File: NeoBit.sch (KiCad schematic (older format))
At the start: 17 parts, among them J2 Barrel_Jack_MountingPin, J5 microbit_edge_connector, U1 74AHCT125, U2 MCP1702-3302E_TO92

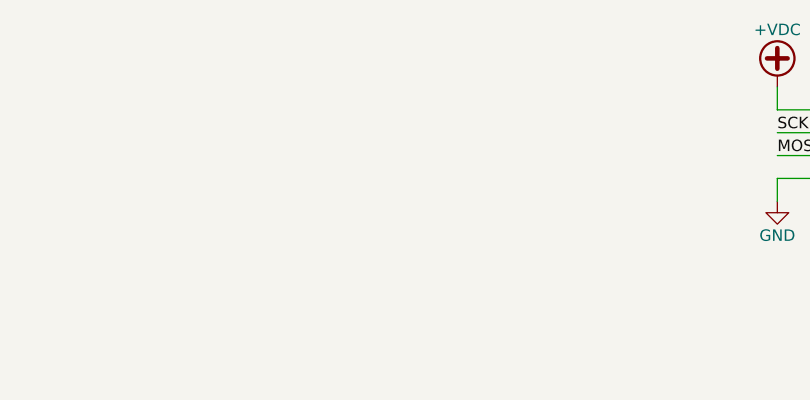
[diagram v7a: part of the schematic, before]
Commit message: Add qwiic connector.
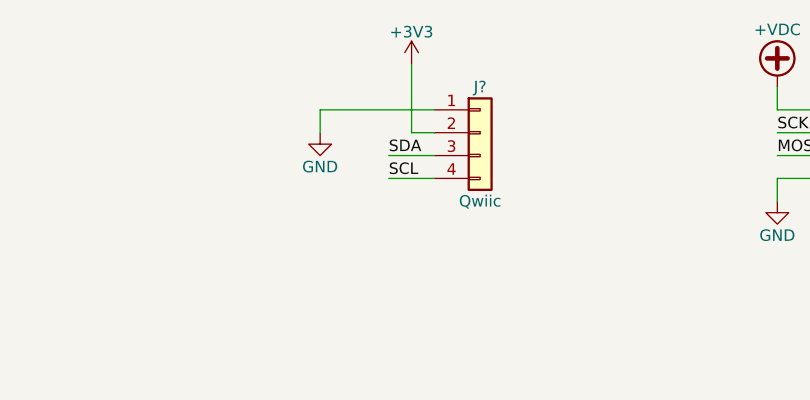
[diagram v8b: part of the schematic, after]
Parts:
- added J?: Qwiic, symbol Conn_01x04
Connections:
- net +3V3: now also J?.2 (Pin_2)
- net GND: now also J?.1 (Pin_1)
- net SCL: now also J?.4 (Pin_4)
- net SDA: now also J?.3 (Pin_3)
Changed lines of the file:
@@
 Wire Wire Line
 	5200 1700 5400 1700
+$Comp
+L Conn_01x04 J?
+U 1 1 5BA3FCC1
+P 3900 1600
+F 0 "J?" H 3900 1800 50  0000 C CNN
+F 1 "Qwiic" H 3900 1300 50  0000 C CNN
+F 2 "" H 3900 1600 50  0001 C CNN
+F 3 "" H 3900 1600 50  0001 C CNN
+	1    3900 1600
+	1    0    0    -1
+$EndComp
+$Comp
+L GND #PWR?
+U 1 1 5BA3FE93
+P 3200 1600
+F 0 "#PWR?" H 3200 1350 50  0001 C CNN
+F 1 "GND" H 3200 1450 50  0000 C CNN
+F 2 "" H 3200 1600 50  0001 C CNN
+F 3 "" H 3200 1600 50  0001 C CNN
+	1    3200 1600
+	1    0    0    -1
+$EndComp
+Wire Wire Line
+	3200 1600 3200 1500
+Wire Wire Line
+	3200 1500 3700 1500
+$Comp
+L +3V3 #PWR?
+U 1 1 5BA3FF8D
+P 3600 1300
+F 0 "#PWR?" H 3600 1150 50  0001 C CNN
+F 1 "+3V3" H 3600 1440 50  0000 C CNN
+F 2 "" H 3600 1300 50  0001 C CNN
+F 3 "" H 3600 1300 50  0001 C CNN
+	1    3600 1300
+	1    0    0    -1
+$EndComp
+Wire Wire Line
+	3700 1600 3600 1600
+Wire Wire Line
+	3600 1600 3600 1300
+Text Label 3500 1700 0    50   ~ 0
+SDA
+Text Label 3500 1800 0    50   ~ 0
+SCL
+Wire Wire Line
+	3500 1700 3700 1700
+Wire Wire Line
+	3500 1800 3700 1800
 $EndSCHEMATC
